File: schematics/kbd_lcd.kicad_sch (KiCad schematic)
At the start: 36 parts, among them J2 Mini-DIN-6, Q1 2N3906, U1 74HC04, U12 74HC04, U13 74HC125, U14 74HC14, U15 NE555P, U16 74HC04, U17 74HC595, U18 80x4 Character LCD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

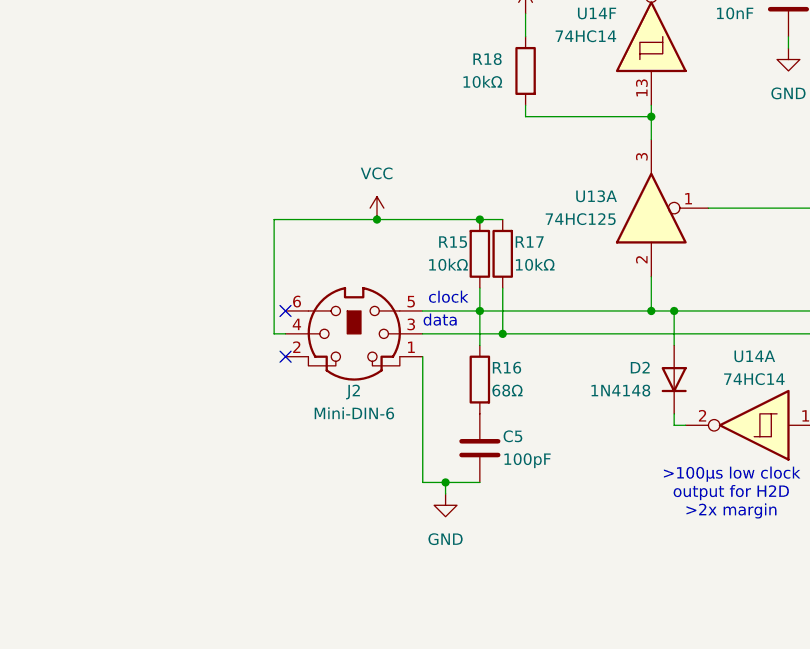
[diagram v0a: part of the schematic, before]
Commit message: improved keyboard termination
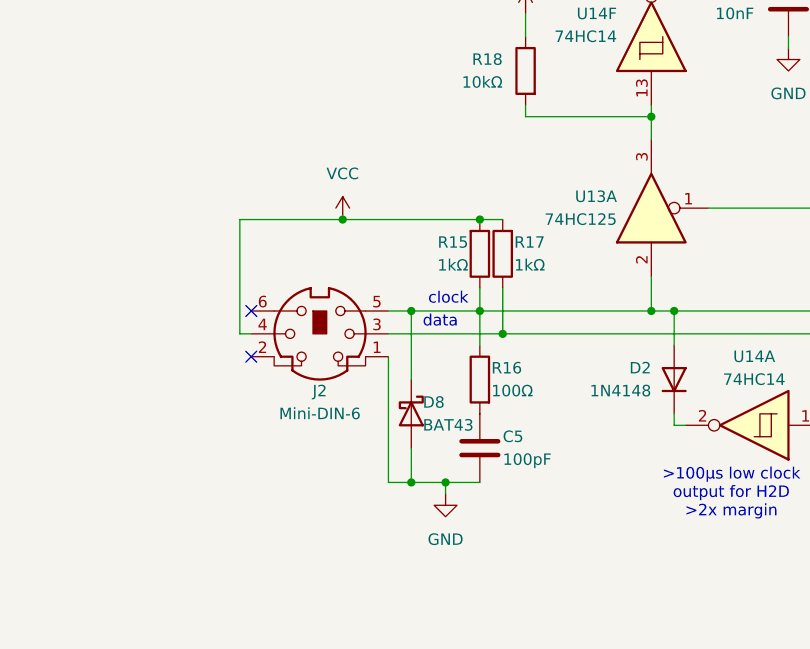
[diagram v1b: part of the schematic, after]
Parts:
- added D8: BAT43, Diode_THT:D_DO-35_SOD27_P7.62mm_Horizontal, symbol Diode:BAT43
- R15, R17: value 10kΩ -> 1kΩ
- R16: value 68Ω -> 100Ω
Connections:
- net GND: now also D8.2 (A)
- net at D2.2 (A), J2.5, R15.1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: now also D8.1 (K)
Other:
- moved on the sheet: J2
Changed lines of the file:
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@@
 	)
 	(junction
+		(at 59.69 71.12)
+		(diameter 0)
+		(color 0 0 0 0)
+	)
+	(junction
 		(at 73.66 172.72)
 		(diameter 0)
@@
 	)
 	(junction
+		(at 55.88 100.33)
+		(diameter 0)
+		(color 0 0 0 0)
+	)
+	(junction
 		(at 115.57 81.28)
 		(diameter 0)
@@
 	)
 	(junction
-		(at 144.78 41.91)
+		(at 62.23 83.82)
 		(diameter 0)
 		(color 0 0 0 0)
 	)
 	(junction
-		(at 60.96 198.12)
+		(at 144.78 41.91)
 		(diameter 0)
 		(color 0 0 0 0)
 	)
 	(junction
-		(at 62.23 83.82)
+		(at 60.96 198.12)
 		(diameter 0)
 		(color 0 0 0 0)
@@
 	)
 	(junction
-		(at 55.88 100.33)
-		(diameter 0)
-		(color 0 0 0 0)
-	)
-	(junction
 		(at 59.69 81.28)
 		(diameter 0)
@@
 	)
 	(junction
+		(at 52.07 81.28)
+		(diameter 0)
+		(color 0 0 0 0)
+	)
+	(junction
 		(at 46.99 -54.61)
 		(diameter 0)
@@
 	)
 	(junction
-		(at 48.26 71.12)
+		(at 44.45 71.12)
 		(diameter 0)
 		(color 0 0 0 0)
@@
 	)
 	(junction
-		(at 148.59 147.32)
+		(at 52.07 100.33)
 		(diameter 0)
 		(color 0 0 0 0)
 	)
 	(junction
-		(at 59.69 71.12)
+		(at 148.59 147.32)
 		(diameter 0)
 		(color 0 0 0 0)
@@
 	)
 	(no_connect
-		(at 38.1 81.28)
+		(at 34.29 81.28)
 	)
 	(no_connect
@@
 	)
 	(no_connect
-		(at 38.1 86.36)
+		(at 34.29 86.36)
 	)
 	(no_connect
@@
 	(wire
 		(pts
-			(xy 36.83 83.82) (xy 38.1 83.82)
+			(xy 33.02 83.82) (xy 34.29 83.82)
 		)
 		(stroke
@@
 	(wire
 		(pts
-			(xy 36.83 71.12) (xy 36.83 83.82)
+			(xy 33.02 71.12) (xy 33.02 83.82)
 		)
 		(stroke
@@
 	(wire
 		(pts
-			(xy 48.26 71.12) (xy 59.69 71.12)
+			(xy 44.45 71.12) (xy 59.69 71.12)
 		)
 		(stroke
@@
 	(wire
 		(pts
-			(xy 53.34 83.82) (xy 62.23 83.82)
+			(xy 49.53 83.82) (xy 62.23 83.82)
 		)
 		(stroke
@@
 	(wire
 		(pts
+			(xy 52.07 96.52) (xy 52.07 100.33)
+		)
+		(stroke
+			(width 0)
+			(type default)
+		)
+	)
+	(wire
+		(pts
 			(xy 59.69 81.28) (xy 78.74 81.28)
 		)
@@
 	(wire
 		(pts
+			(xy 52.07 81.28) (xy 59.69 81.28)
+		)
+		(stroke
+			(width 0)
+			(type default)
+		)
+	)
+	(wire
+		(pts
 			(xy 115.57 53.34) (xy 115.57 41.91)
 		)
@@
 	(wire
 		(pts
-			(xy 53.34 100.33) (xy 55.88 100.33)
+			(xy 49.53 100.33) (xy 52.07 100.33)
 		)
 		(stroke
@@
 	(wire
 		(pts
+			(xy 52.07 100.33) (xy 55.88 100.33)
+		)
+		(stroke
+			(width 0)
+			(type default)
+		)
+	)
+	(wire
+		(pts
 			(xy 119.38 93.98) (xy 119.38 109.22)
 		)
@@
 	(wire
 		(pts
-			(xy 53.34 81.28) (xy 59.69 81.28)
+			(xy 49.53 81.28) (xy 52.07 81.28)
 		)
 		(stroke
@@
 	(wire
 		(pts
+			(xy 52.07 81.28) (xy 52.07 88.9)
+		)
+		(stroke
+			(width 0)
+			(type default)
+		)
+	)
+	(wire
+		(pts
 			(xy 189.23 40.64) (xy 208.28 40.64)
 		)
@@
 	(wire
 		(pts
-			(xy 53.34 86.36) (xy 53.34 100.33)
+			(xy 49.53 86.36) (xy 49.53 100.33)
 		)
 		(stroke
@@
 	(wire
 		(pts
-			(xy 36.83 71.12) (xy 48.26 71.12)
+			(xy 33.02 71.12) (xy 44.45 71.12)
 		)
 		(stroke
@@
 	(symbol
 		(lib_id "Connector:Mini-DIN-6")
-		(at 45.72 83.82 0)
+		(at 41.91 83.82 0)
 		(unit 1)
 		(body_style 1)
@@
 		(dnp no)
 		(property "Reference" "J2"
-			(at 45.72 90.17 0)
+			(at 41.91 90.17 0)
 			(show_name no)
 			(do_not_autoplace no)
@@
 		)
 		(property "Value" "Mini-DIN-6"
-			(at 45.72 92.71 0)
+			(at 41.91 92.71 0)
 			(show_name no)
 			(do_not_autoplace no)
@@
 		)
 		(property "Footprint" ""
-			(at 45.72 83.82 0)
+			(at 41.91 83.82 0)
 			(hide yes)
 			(show_name no)
@@
 		)
 		(property "Datasheet" "http://service.powerdynamics.com/ec/Catalog17/Section%2011.pdf"
-			(at 45.72 83.82 0)
+			(at 41.91 83.82 0)
 			(hide yes)
 			(show_name no)
@@
 		)
 		(property "Description" "6-pin Mini-DIN connector"
-			(at 45.72 83.82 0)
+			(at 41.91 83.82 0)
 			(hide yes)
 			(show_name no)
@@
 			)
 		)
-		(property "Value" "10kΩ"
+		(property "Value" "1kΩ"
 			(at 63.5 76.2 0)
 			(show_name no)
@@
 			)
 		)
-		(property "Value" "10kΩ"
+		(property "Value" "1kΩ"
 			(at 58.42 76.2 0)
 			(show_name no)
@@
 	(symbol
 		(lib_id "power:VCC")
-		(at 48.26 71.12 0)
+		(at 44.45 71.12 0)
 		(unit 1)
 		(body_style 1)
@@
 		(dnp no)
 		(property "Reference" "#PWR027"
-			(at 48.26 74.93 0)
+			(at 44.45 74.93 0)
 			(hide yes)
 			(show_name no)
@@
 		)
 		(property "Value" "VCC"
-			(at 48.26 66.04 0)
+			(at 44.45 66.04 0)
 			(show_name no)
 			(do_not_autoplace no)
@@
 		)
 		(property "Footprint" ""
-			(at 48.26 71.12 0)
+			(at 44.45 71.12 0)
 			(hide yes)
 			(show_name no)
@@
 		)
 		(property "Datasheet" ""
-			(at 48.26 71.12 0)
+			(at 44.45 71.12 0)
 			(hide yes)
 			(show_name no)
@@
 		)
 		(property "Description" "Power symbol creates a global label with name \"VCC\""
-			(at 48.26 71.12 0)
+			(at 44.45 71.12 0)
 			(hide yes)
 			(show_name no)
@@
 			)
 		)
-		(property "Value" "68Ω"
+		(property "Value" "100Ω"
 			(at 60.96 90.17 0)
 			(show_name no)
@@
 				)
 			)
+		)
+	)
+	(symbol
+		(lib_id "Diode:BAT43")
+		(at 52.07 92.71 270)
+		(unit 1)
+		(body_style 1)
+		(exclude_from_sim no)
+		(in_bom yes)
+		(on_board yes)
+		(in_pos_files yes)
+		(dnp no)
+		(property "Reference" "D8"
+			(at 53.34 91.44 90)
+			(show_name no)
+			(do_not_autoplace no)
+			(effects
+				(font
+					(size 1.27 1.27)
+				)
+				(justify left)
+			)
+		)
+		(property "Value" "BAT43"
+			(at 53.34 93.98 90)
+			(show_name no)
+			(do_not_autoplace no)
+			(effects
+				(font
+					(size 1.27 1.27)
+				)
+				(justify left)
+			)
+		)
+		(property "Footprint" "Diode_THT:D_DO-35_SOD27_P7.62mm_Horizontal"
+			(at 47.625 92.71 0)
+			(hide yes)
+			(show_name no)
+			(do_not_autoplace no)
+			(effects
+				(font
+					(size 1.27 1.27)
+				)
+			)
+		)
+		(property "Datasheet" "http://www.vishay.com/docs/85660/bat42.pdf"
+			(at 52.07 92.71 0)
+			(hide yes)
+			(show_name no)
+			(do_not_autoplace no)
+			(effects
+				(font
+					(size 1.27 1.27)
+				)
+			)
+		)
+		(property "Description" "30V 0.2A Small Signal Schottky Diode, DO-35"
+			(at 52.07 92.71 0)
+			(hide yes)
+			(show_name no)
+			(do_not_autoplace no)
+			(effects
+				(font
+					(size 1.27 1.27)
+				)
+			)
+		)
+		(pin "2"
+		)
+		(pin "1"
+		)
+		(instances
+			(project "bv6502_hw"
+				(path "/94c72abe-aaa5-49aa-8ab7-5d3e7cbc10be/3a12e717-ce5f-4719-9e29-095356b3ec50"
+					(reference "D8")
+					(unit 1)
+				)
+			)

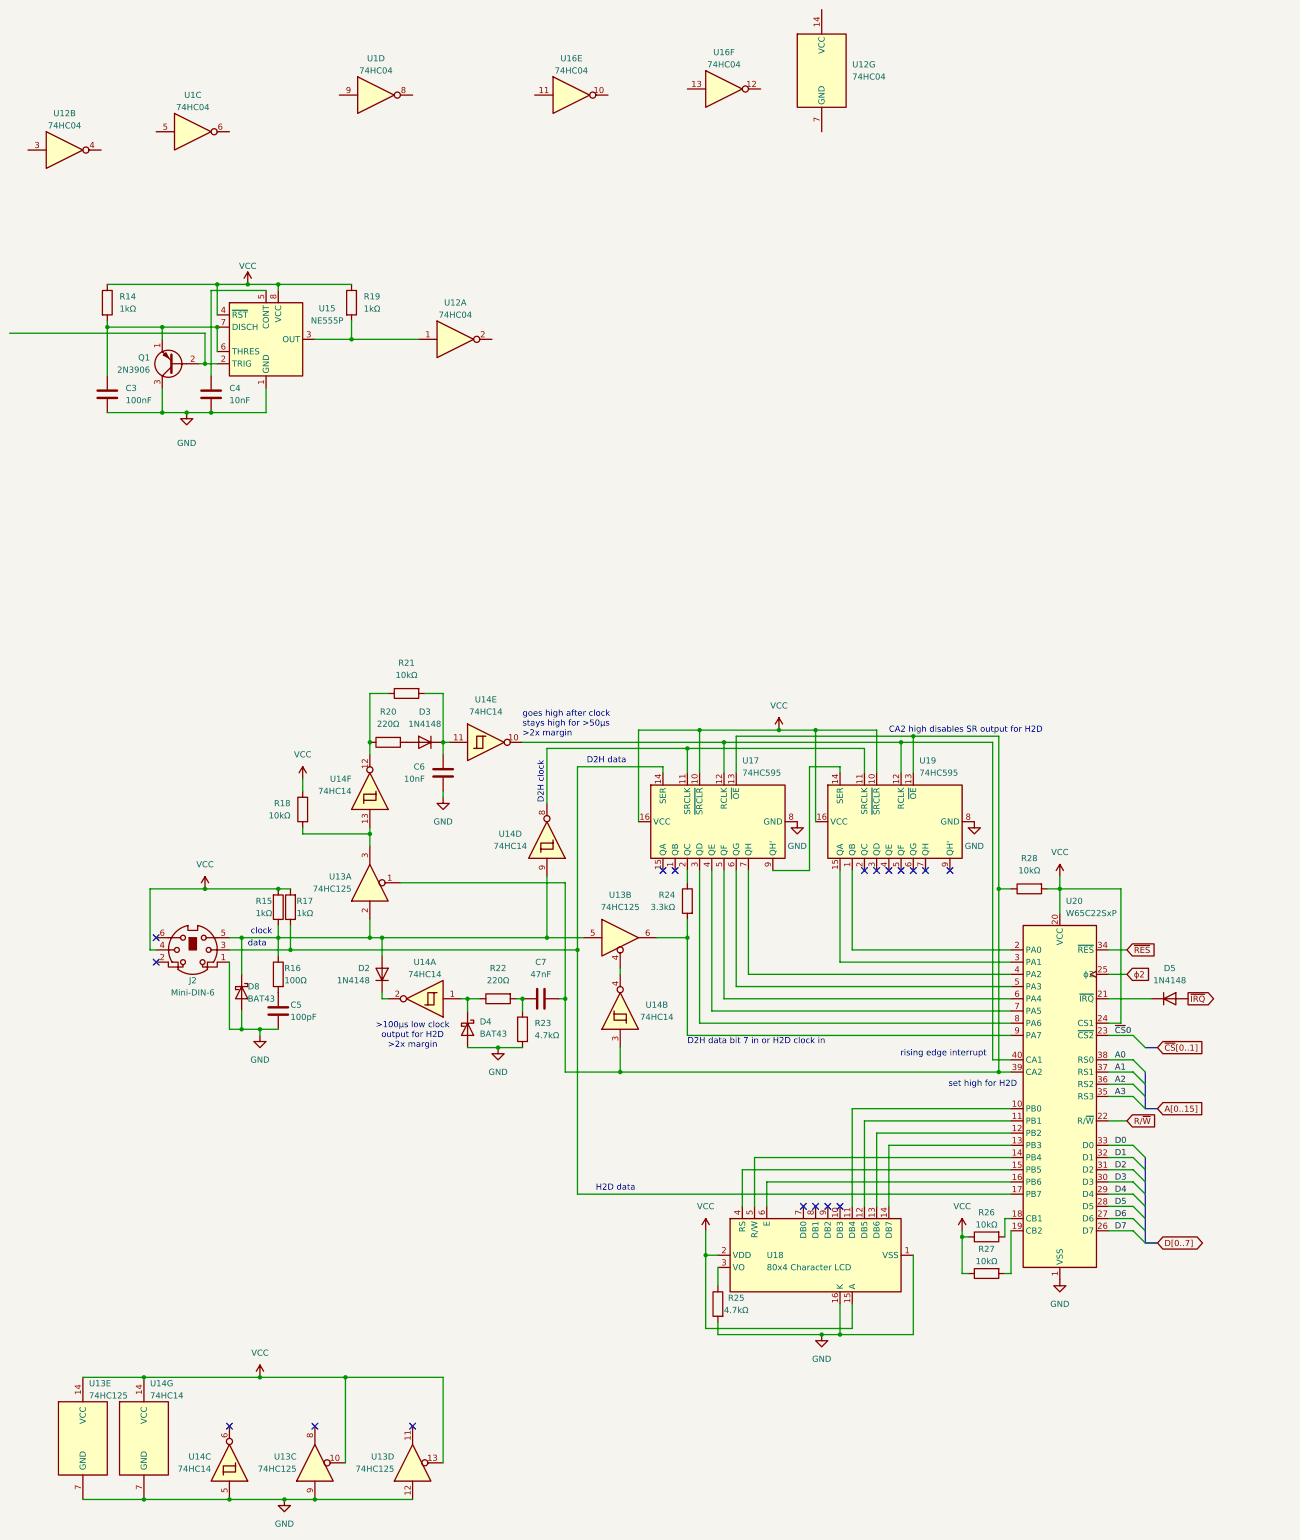
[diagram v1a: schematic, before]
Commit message: line wrap fixes, keyboard rewire due to slow rise time
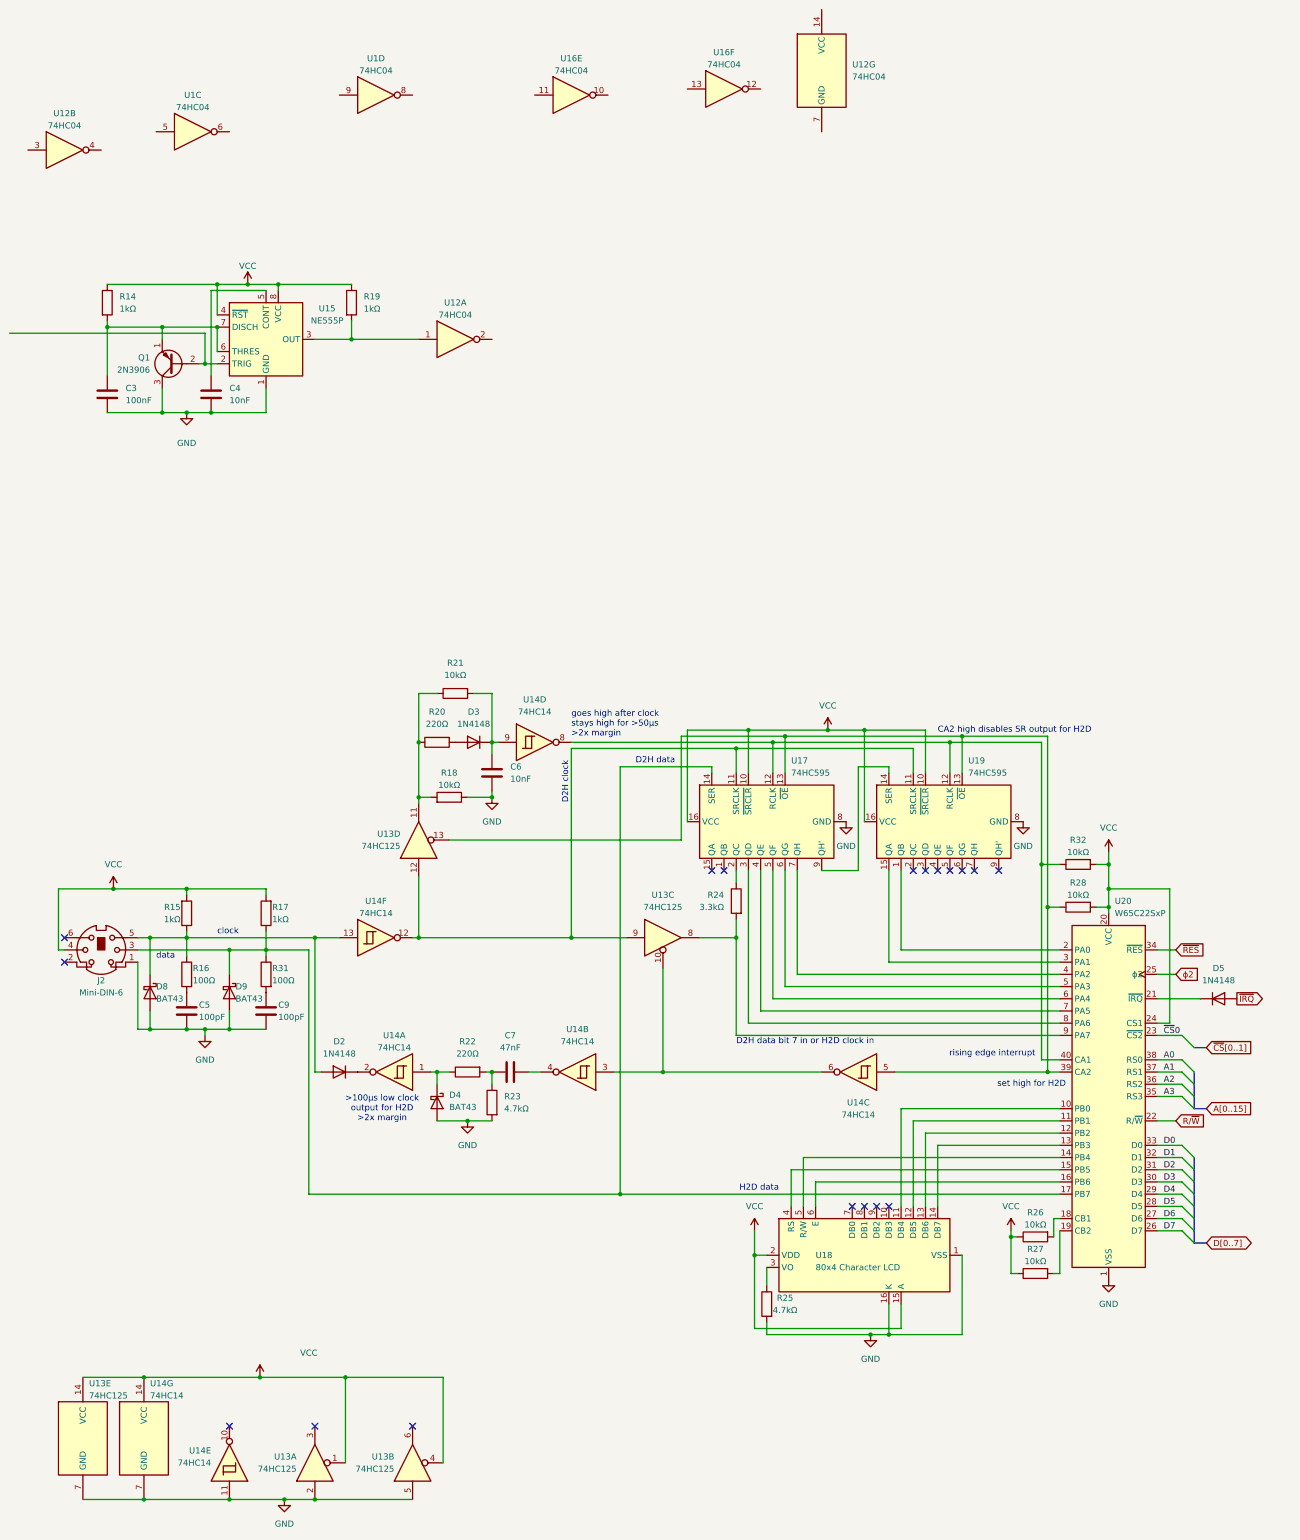
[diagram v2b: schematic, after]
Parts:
- removed unit 4 of U14
- added C9: 100pF, symbol Device:C
- added D9: BAT43, Diode_THT:D_DO-35_SOD27_P7.62mm_Horizontal, symbol Diode:BAT43
- added R31: 100Ω, symbol Device:R
- added R32: 10kΩ, symbol Device:R
- added unit 5 of U14
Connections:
- net GND: now also R18.1, U13.2, U13.5, C9.2, D9.2 (A), U14.11; no longer U13.12, U13.9, U14.5
- net VCC: now also U13.1, U13.4, R32.2; no longer R18.1, U13.10, U13.13
- net at R28.1, U17.13 (~{OE}), U19.13 (~{OE})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: now also U13.13, U14.5; no longer C7.2, U13.1, U14.3
- net at D2.2 (A), D8.1 (K), J2.5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: now also U14.13; no longer U13.2, U13.5
- net at U14.6: now also U13.10, U14.3
- net at J2.3, R17.1, U17.14 (SER)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: now also D9.1 (K), R31.1
- net at U17.12 (RCLK), U19.12 (RCLK), U20.40 (CA1): now also U14.8, R32.1; no longer U14.10
- net at R24.2, U20.9 (PA7): now also U13.8; no longer U13.6
- net at U17.11 (SRCLK), U19.11 (SRCLK): now also U13.12, U13.9, U14.12
- net at R20.1, R21.1: now also R18.2, U13.11; no longer U14.12
- net at C6.1, D3.1 (K), R21.2: now also U14.9; no longer U14.11
- net at U14.4: now also C7.2; no longer U13.4
- new net: C9.1, R31.2
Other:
- moved on the sheet: C5, C6, C7, D2, D3, D4, D5, D8, J2, R15, R16, R17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
